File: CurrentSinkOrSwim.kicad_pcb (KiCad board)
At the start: 2 copper layers, 48.3 x 52.1 mm, 23 parts, among them P1 CONN_01X01, P101 CONN_01X02, P102 CONN_01X03, P103 CONN_01X02, Q401 BUK9575, U201 LMV358, U301 LM2931D-R

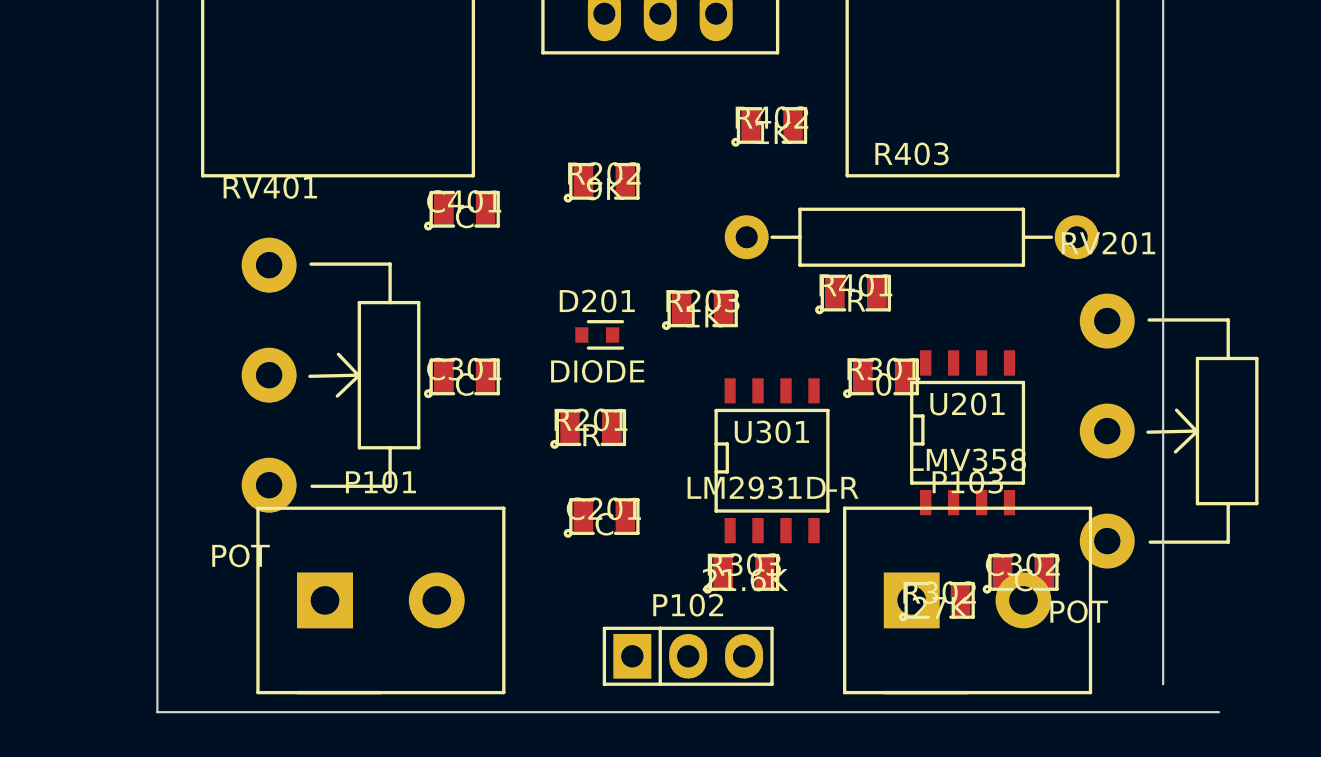
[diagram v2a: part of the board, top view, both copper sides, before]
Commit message: Cosmetic cleanup of schematic
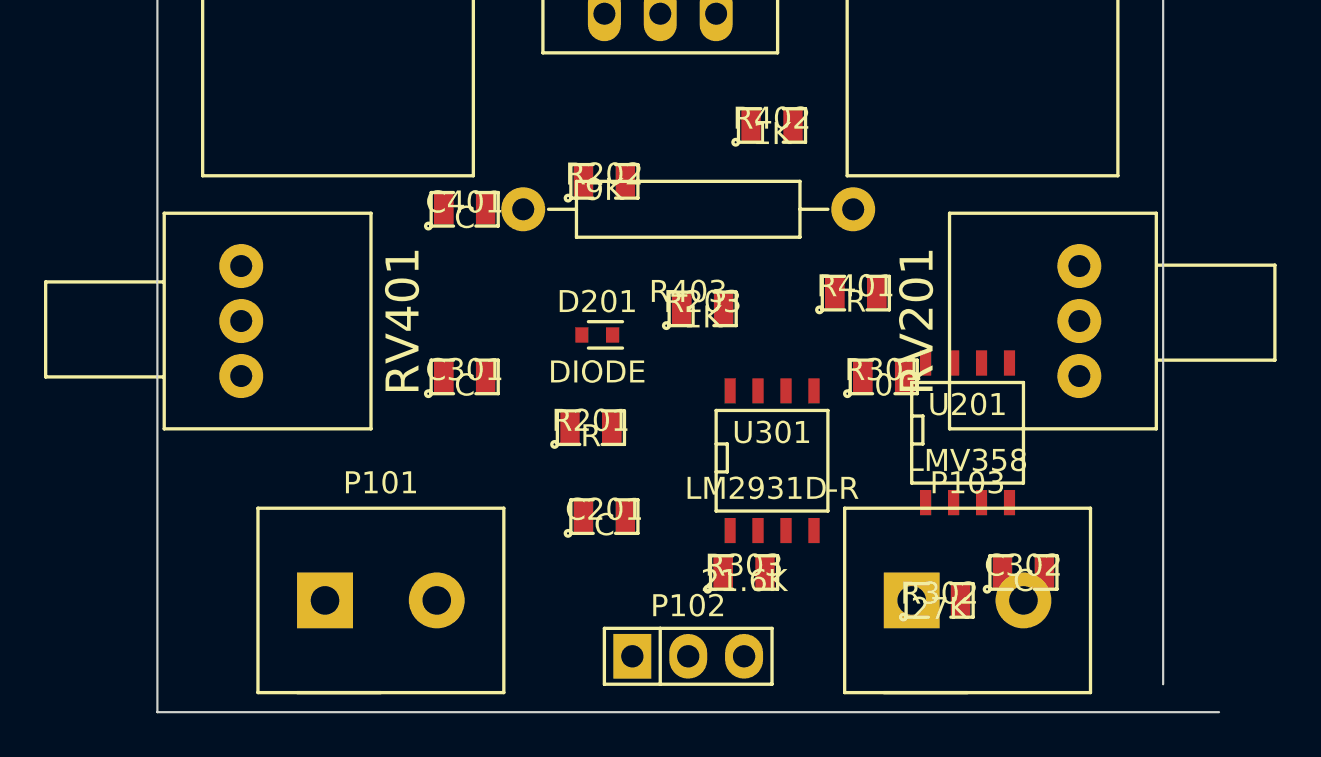
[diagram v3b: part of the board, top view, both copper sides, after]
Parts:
- RV201, RV401: footprint Potentiometers:Potentiometer_WirePads_largePads -> Current:P090L-02F25BR10K
- moved R403 10.2 mm to (128.3, 62.2), turned to 180 degrees
- moved RV401 2.84 mm to (108.0, 67.3), turned to 270 degrees
- moved RV201 1.27 mm to (146.1, 67.3), turned to 90 degrees
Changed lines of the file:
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@@
 (kicad_pcb (version 4) (host pcbnew 0.201502091101+5410~21~ubuntu14.04.1-product)
   (general
-    (links 43)
-    (no_connects 43)
+    (links 41)
+    (no_connects 41)
     (area 104.089999 32.969999 152.450001 85.140001)
     (thickness 1.6)
@@
     (zones 0)
     (modules 23)
-    (nets 18)
+    (nets 16)
   )
   (page A4)
@@
   (net 14 "Net-(R401-Pad1)")
   (net 15 "Net-(R402-Pad2)")
-  (net 16 "Net-(RV201-Pad1)")
-  (net 17 "Net-(RV401-Pad1)")
   (net_class Default "This is the default net class."
     (clearance 0.254)
@@
     (add_net "Net-(R401-Pad1)")
     (add_net "Net-(R402-Pad2)")
-    (add_net "Net-(RV201-Pad1)")
-    (add_net "Net-(RV401-Pad1)")
   )
   (module SMD_Packages:SMD-0805 (layer F.Cu)
@@
   )
   (module Resistors_ThroughHole:Resistor_Horizontal_RM15mm (layer F.Cu)
-    (at 138.43 63.5)
+    (at 128.27 62.23 180)
     (descr "Resistor, Axial, RM 15mm,")
     (tags "Resistor, Axial, RM 15mm,")
-    (fp_text reference R403 (at 0 -3.74904) (layer F.SilkS)
-      (effects (font (size 1 1) (thickness 0.15)))
-    )
-    (fp_text value .1 (at 0 4.0005) (layer F.SilkS) hide
+    (fp_text reference R403 (at 0 -3.74904 180) (layer F.SilkS)
+      (effects (font (size 1 1) (thickness 0.15)))
+    )
+    (fp_text value .1 (at 0 4.0005 180) (layer F.SilkS) hide
       (effects (font (size 1 1) (thickness 0.15)))
     )
@@
     (fp_line (start 6.35 0) (end 5.08 0) (layer F.SilkS) (width 0.15))
     (fp_line (start -6.35 0) (end -5.08 0) (layer F.SilkS) (width 0.15))
-    (pad 1 thru_hole circle (at -7.5 0) (size 1.99898 1.99898) (drill 1.00076) (layers *.Cu *.SilkS *.Mask)
+    (pad 1 thru_hole circle (at -7.5 0 180) (size 1.99898 1.99898) (drill 1.00076) (layers *.Cu *.SilkS *.Mask)
       (net 8 "Net-(Q401-PadS)"))
-    (pad 2 thru_hole circle (at 7.5 0) (size 1.99898 1.99898) (drill 1.00076) (layers *.Cu *.SilkS *.Mask)
+    (pad 2 thru_hole circle (at 7.5 0 180) (size 1.99898 1.99898) (drill 1.00076) (layers *.Cu *.SilkS *.Mask)
       (net 2 GND))
     (model Resistors_ThroughHole/Resistor_Horizontal_RM15mm.wrl
@@
       (rotate (xyz 0 0 0))
     )
-  )
-  (module Potentiometers:Potentiometer_WirePads_largePads (layer F.Cu)
-    (at 147.32 67.31)
-    (descr "Potentiometer, Wire Pads only, RevA, 30 July 2010,")
-    (tags "Potentiometer, Wire Pads only, RevA, 30 July 2010,")
-    (fp_text reference RV201 (at 0.0508 -3.49758) (layer F.SilkS)
-      (effects (font (size 1 1) (thickness 0.15)))
-    )
-    (fp_text value POT (at -1.34874 13.25118) (layer F.SilkS)
-      (effects (font (size 1 1) (thickness 0.15)))
-    )
-    (fp_line (start 5.4991 10.05078) (end 1.95072 10.05078) (layer F.SilkS) (width 0.15))
-    (fp_line (start 5.4991 8.30072) (end 5.4991 10.05078) (layer F.SilkS) (width 0.15))
-    (fp_line (start 5.4991 1.7018) (end 5.4991 -0.04826) (layer F.SilkS) (width 0.15))
-    (fp_line (start 5.4991 -0.04826) (end 1.89992 -0.04826) (layer F.SilkS) (width 0.15))
-    (fp_line (start 4.09956 5.00126) (end 1.84912 5.05206) (layer F.SilkS) (width 0.15))
-    (fp_line (start 4.09956 5.00126) (end 3.0988 5.95122) (layer F.SilkS) (width 0.15))
-    (fp_line (start 4.09956 5.05206) (end 3.1496 4.0513) (layer F.SilkS) (width 0.15))
-    (fp_line (start 4.09956 1.7018) (end 6.79958 1.7018) (layer F.SilkS) (width 0.15))
-    (fp_line (start 6.79958 1.7018) (end 6.79958 8.30072) (layer F.SilkS) (width 0.15))
-    (fp_line (start 6.79958 8.30072) (end 4.09956 8.30072) (layer F.SilkS) (width 0.15))
-    (fp_line (start 4.09956 8.30072) (end 4.09956 1.7018) (layer F.SilkS) (width 0.15))
-    (pad 2 thru_hole circle (at 0 5.00126) (size 2.49936 2.49936) (drill 1.19888) (layers *.Cu *.Mask F.SilkS)
-      (net 1 2.7V))
-    (pad 3 thru_hole circle (at 0 10.00252) (size 2.49936 2.49936) (drill 1.19888) (layers *.Cu *.Mask F.SilkS)
-      (net 9 "Net-(R201-Pad1)"))
-    (pad 1 thru_hole circle (at 0 0) (size 2.49936 2.49936) (drill 1.19888) (layers *.Cu *.Mask F.SilkS)
-      (net 16 "Net-(RV201-Pad1)"))
-  )
-  (module Potentiometers:Potentiometer_WirePads_largePads (layer F.Cu)
-    (at 109.22 64.77)
-    (descr "Potentiometer, Wire Pads only, RevA, 30 July 2010,")
-    (tags "Potentiometer, Wire Pads only, RevA, 30 July 2010,")
-    (fp_text reference RV401 (at 0.0508 -3.49758) (layer F.SilkS)
-      (effects (font (size 1 1) (thickness 0.15)))
-    )
-    (fp_text value POT (at -1.34874 13.25118) (layer F.SilkS)
-      (effects (font (size 1 1) (thickness 0.15)))
-    )
-    (fp_line (start 5.4991 10.05078) (end 1.95072 10.05078) (layer F.SilkS) (width 0.15))
-    (fp_line (start 5.4991 8.30072) (end 5.4991 10.05078) (layer F.SilkS) (width 0.15))
-    (fp_line (start 5.4991 1.7018) (end 5.4991 -0.04826) (layer F.SilkS) (width 0.15))
-    (fp_line (start 5.4991 -0.04826) (end 1.89992 -0.04826) (layer F.SilkS) (width 0.15))
-    (fp_line (start 4.09956 5.00126) (end 1.84912 5.05206) (layer F.SilkS) (width 0.15))
-    (fp_line (start 4.09956 5.00126) (end 3.0988 5.95122) (layer F.SilkS) (width 0.15))
-    (fp_line (start 4.09956 5.05206) (end 3.1496 4.0513) (layer F.SilkS) (width 0.15))
-    (fp_line (start 4.09956 1.7018) (end 6.79958 1.7018) (layer F.SilkS) (width 0.15))
-    (fp_line (start 6.79958 1.7018) (end 6.79958 8.30072) (layer F.SilkS) (width 0.15))
-    (fp_line (start 6.79958 8.30072) (end 4.09956 8.30072) (layer F.SilkS) (width 0.15))
-    (fp_line (start 4.09956 8.30072) (end 4.09956 1.7018) (layer F.SilkS) (width 0.15))
-    (pad 2 thru_hole circle (at 0 5.00126) (size 2.49936 2.49936) (drill 1.19888) (layers *.Cu *.Mask F.SilkS)
-      (net 1 2.7V))
-    (pad 3 thru_hole circle (at 0 10.00252) (size 2.49936 2.49936) (drill 1.19888) (layers *.Cu *.Mask F.SilkS)
-      (net 14 "Net-(R401-Pad1)"))
-    (pad 1 thru_hole circle (at 0 0) (size 2.49936 2.49936) (drill 1.19888) (layers *.Cu *.Mask F.SilkS)
-      (net 17 "Net-(RV401-Pad1)"))
   )
   (module SMD_Packages:SOIC-8-N (layer F.Cu)
@@
     )
   )
+  (module Current:P090L-02F25BR10K (layer F.Cu)
+    (at 146.05 67.31 90)
+    (fp_text reference RV201 (at 0 -7.366 90) (layer F.SilkS)
+      (effects (font (size 1.5 1.5) (thickness 0.15)))
+    )
+    (fp_text value POT (at 0 -9.906 90) (layer F.Fab)
+      (effects (font (size 1.5 1.5) (thickness 0.15)))
+    )
+    (fp_line (start -1.778 3.556) (end -1.778 8.89) (layer F.SilkS) (width 0.15))
+    (fp_line (start -1.778 8.89) (end 2.54 8.89) (layer F.SilkS) (width 0.15))
+    (fp_line (start 2.54 8.89) (end 2.54 3.556) (layer F.SilkS) (width 0.15))
+    (fp_line (start -4.9 -5.9) (end 4.9 -5.9) (layer F.SilkS) (width 0.15))
+    (fp_line (start -4.9 3.5) (end 4.9 3.5) (layer F.SilkS) (width 0.15))
+    (fp_line (start 4.9 -5.9) (end 4.9 3.5) (layer F.SilkS) (width 0.15))
+    (fp_line (start -4.9 -5.9) (end -4.9 3.5) (layer F.SilkS) (width 0.15))
+    (pad 3 thru_hole circle (at 2.5 0 90) (size 2 2) (drill 1) (layers *.Cu *.Mask F.SilkS)
+      (net 9 "Net-(R201-Pad1)"))
+    (pad 4 thru_hole circle (at 0 0 90) (size 2 2) (drill 1) (layers *.Cu *.Mask F.SilkS))
+    (pad 5 thru_hole circle (at -2.5 0 90) (size 2 2) (drill 1) (layers *.Cu *.Mask F.SilkS))
+    (pad "" np_thru_hole oval (at 5.1 -3.3 90) (size 2 2.2) (drill oval 2 2.2) (layers *.Cu *.Mask F.SilkS))
+    (pad "" np_thru_hole oval (at -5.1 -3.3 90) (size 2 2.2) (drill oval 2 2.2) (layers *.Cu *.Mask F.SilkS))
+  )
+  (module Current:P090L-02F25BR10K (layer F.Cu)
+    (at 107.95 67.31 270)
+    (fp_text reference RV401 (at 0 -7.366 270) (layer F.SilkS)
+      (effects (font (size 1.5 1.5) (thickness 0.15)))
+    )
+    (fp_text value POT (at 0 -9.906 270) (layer F.Fab)
+      (effects (font (size 1.5 1.5) (thickness 0.15)))
+    )
+    (fp_line (start -1.778 3.556) (end -1.778 8.89) (layer F.SilkS) (width 0.15))
+    (fp_line (start -1.778 8.89) (end 2.54 8.89) (layer F.SilkS) (width 0.15))
+    (fp_line (start 2.54 8.89) (end 2.54 3.556) (layer F.SilkS) (width 0.15))
+    (fp_line (start -4.9 -5.9) (end 4.9 -5.9) (layer F.SilkS) (width 0.15))
+    (fp_line (start -4.9 3.5) (end 4.9 3.5) (layer F.SilkS) (width 0.15))
+    (fp_line (start 4.9 -5.9) (end 4.9 3.5) (layer F.SilkS) (width 0.15))
+    (fp_line (start -4.9 -5.9) (end -4.9 3.5) (layer F.SilkS) (width 0.15))
+    (pad 3 thru_hole circle (at 2.5 0 270) (size 2 2) (drill 1) (layers *.Cu *.Mask F.SilkS)
+      (net 14 "Net-(R401-Pad1)"))
+    (pad 4 thru_hole circle (at 0 0 270) (size 2 2) (drill 1) (layers *.Cu *.Mask F.SilkS))
+    (pad 5 thru_hole circle (at -2.5 0 270) (size 2 2) (drill 1) (layers *.Cu *.Mask F.SilkS))
+    (pad "" np_thru_hole oval (at 5.1 -3.3 270) (size 2 2.2) (drill oval 2 2.2) (layers *.Cu *.Mask F.SilkS))
+    (pad "" np_thru_hole oval (at -5.1 -3.3 270) (size 2 2.2) (drill oval 2 2.2) (layers *.Cu *.Mask F.SilkS))
+  )
   (gr_line (start 152.4 34.29) (end 104.14 34.29) (angle 90) (layer Edge.Cuts) (width 0.1))

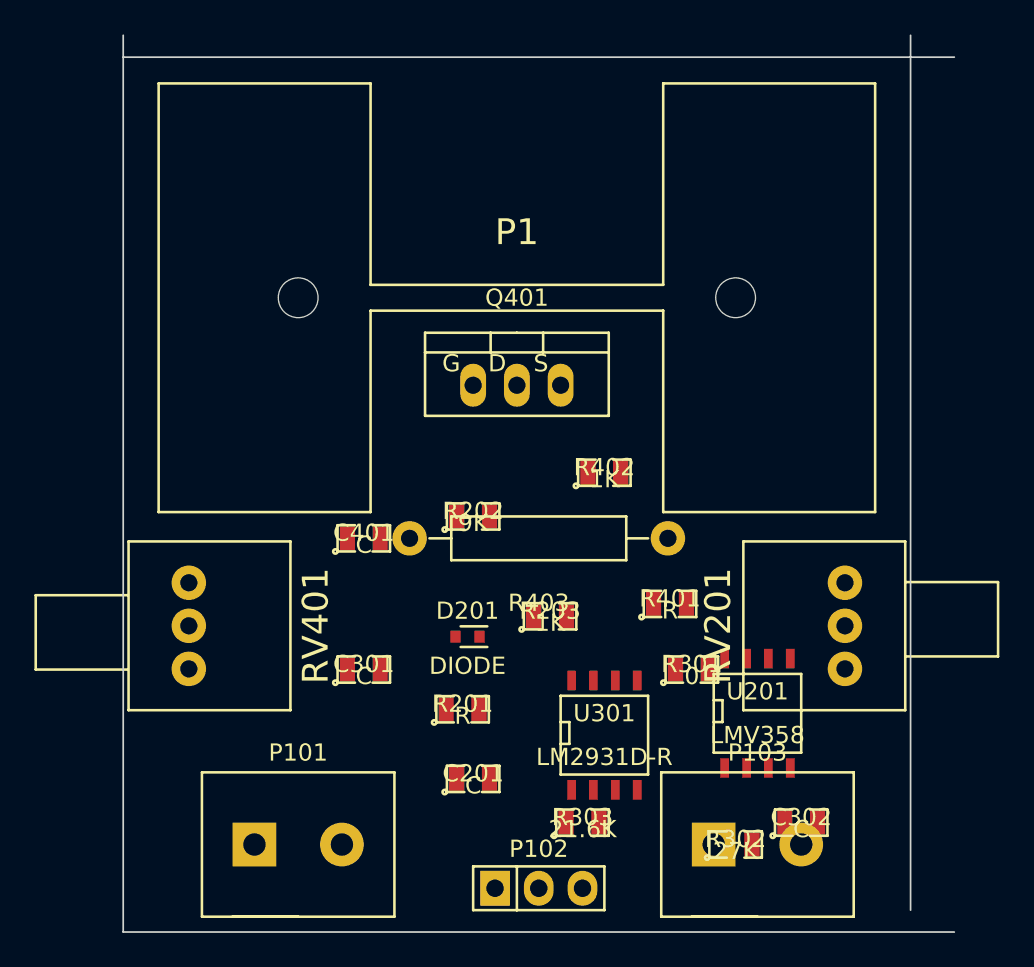
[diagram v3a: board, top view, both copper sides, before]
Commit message: Added keep out and did initial placement
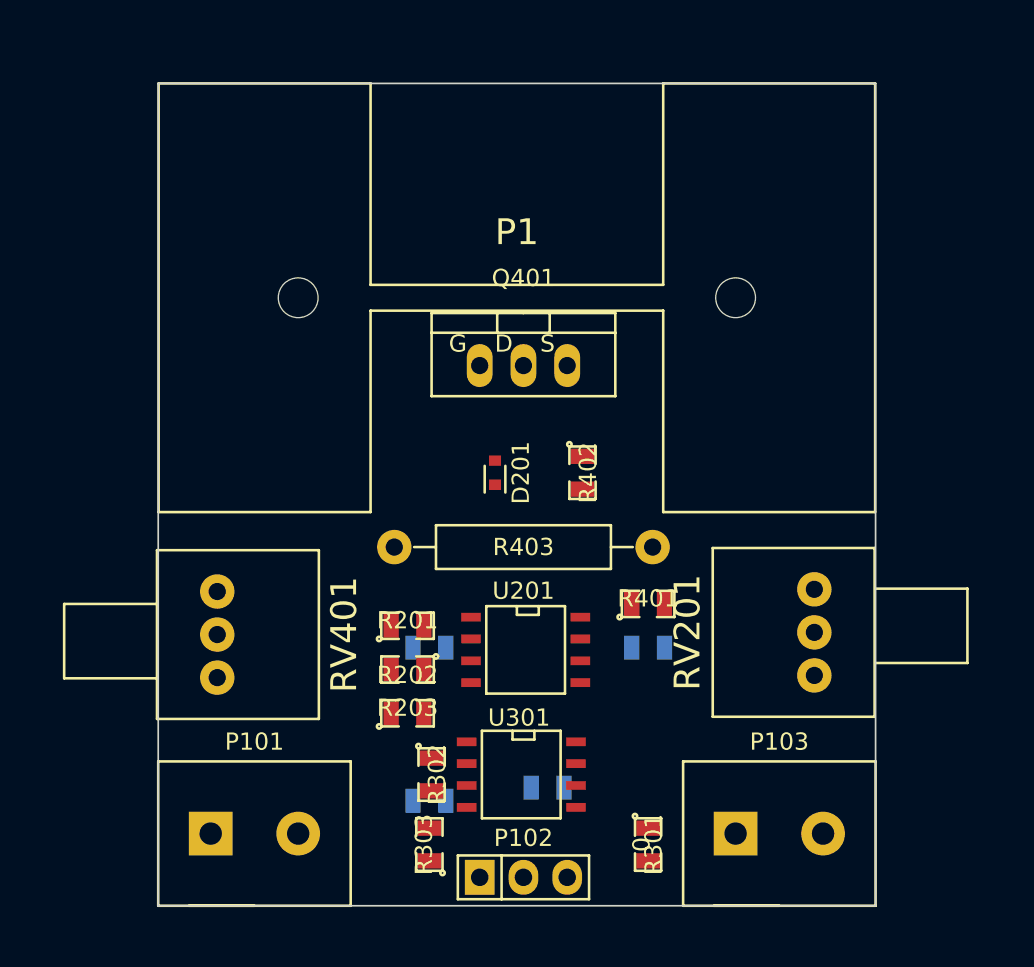
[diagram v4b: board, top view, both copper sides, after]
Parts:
- C201, C301, C302, C401: moved to B.Cu
- R201: value R -> 28.7K
- R401: value R -> 68K
- RV201, RV401: value POT -> 10K
- moved R302 18.1 mm to (122.0, 75.9), turned to 270 degrees
- moved C401 17.7 mm to (134.6, 68.6)
- moved C302 14.9 mm to (128.8, 76.7)
- moved U201 14.0 mm to (127.5, 68.7), turned to 270 degrees
- moved R301 10.5 mm to (134.6, 80.0), turned to 270 degrees
- moved R203 10.0 mm to (120.7, 72.4)
- moved R202 9.67 mm to (120.7, 69.8), turned to 180 degrees
- moved D201 9.65 mm to (125.7, 58.4), turned to 270 degrees
- moved R303 8.98 mm to (121.9, 80.0), turned to 90 degrees
- moved R201 5.81 mm to (120.7, 67.3)
- moved U301 5.34 mm to (127.3, 75.9), turned to 270 degrees
- moved C301 4.02 mm to (121.9, 68.6)
- moved C201 2.84 mm to (121.9, 77.5)
- moved P101 2.62 mm to (111.8, 79.4)
- moved RV201 1.82 mm to (144.3, 67.7)
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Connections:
- R201 pad 1: Net-(R201-Pad1) -> 2.7V
- R201 pad 2: /Voltage Control/Current_Sink- -> Net-(R201-Pad2)
- R401 pad 1: Net-(R401-Pad1) -> 2.7V
- R401 pad 2: GND -> Net-(R401-Pad2)
- RV201 pad 3: Net-(R201-Pad1) -> /Voltage Control/Current_Sink-
- RV401 pad 3: Net-(R401-Pad1) -> Net-(RV401-Pad3)
- U201 pad 3: Net-(R201-Pad1) -> Net-(R201-Pad2)
- U201 pad 5: Net-(R401-Pad1) -> Net-(R401-Pad2)
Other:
- board size 48.3 x 52.1 mm -> 41.7 x 47.8 mm

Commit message: CSOS Layout session 1
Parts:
- moved RV201 34.7 mm to (109.6, 67.6), turned to 270 degrees
- moved RV401 33.8 mm to (143.4, 68.2), turned to 90 degrees
- moved C301 12.1 mm to (133.3, 72.5)
- moved C302 8.46 mm to (121.2, 73.0), turned to 180 degrees
- moved R301 3.56 mm to (134.7, 76.5), turned to 90 degrees
- moved R303 1.49 mm to (121.4, 78.6), turned to 270 degrees
- moved R302 1.09 mm to (121.4, 75.1)
- moved R403 0.97 mm to (126.5, 63.1)
- moved U201 0.80 mm to (127.3, 67.9)
- moved P102 0.40 mm to (127.3, 81.5)
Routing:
- net /Current Control/Current_Sink+: track 0.00 -> 63.6 mm
- net Net-(P101-Pad1): track 0.00 -> 17.1 mm
- net /Power Regulation/Vin: track 0.00 -> 13.6 mm, vias 0 -> 1
- net GND: track 0.00 -> 7.60 mm, vias 0 -> 1
- net Net-(R301-Pad1): track 0.00 -> 4.50 mm
- net Net-(R302-Pad2): track 0.00 -> 4.40 mm
- net 2.7V: track 0.00 -> 2.69 mm
- added copper zone on B.Cu, net GND
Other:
- net class Power added: clearance 0.3048, trace_width 0.6096, via_dia 1.143, via_drill 0.762
